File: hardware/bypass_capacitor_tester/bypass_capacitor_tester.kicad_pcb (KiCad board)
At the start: 2 copper layers, 40 x 34 mm, 13 parts, among them J1 Coax, J2 Coax, J3 Coax, J4 Conn_01x02, Q1 MMBT2369AL

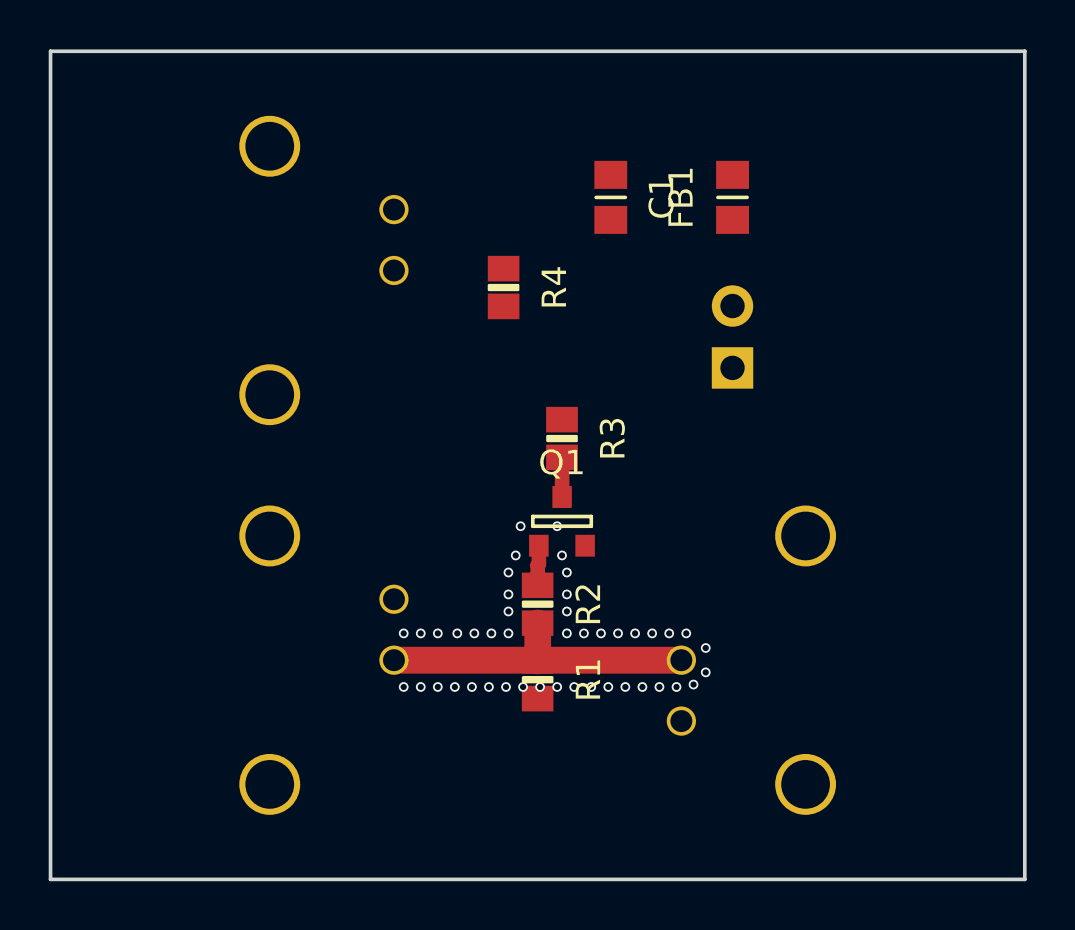
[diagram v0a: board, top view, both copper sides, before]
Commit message: changed coaxial connectors to SMA edge connectors
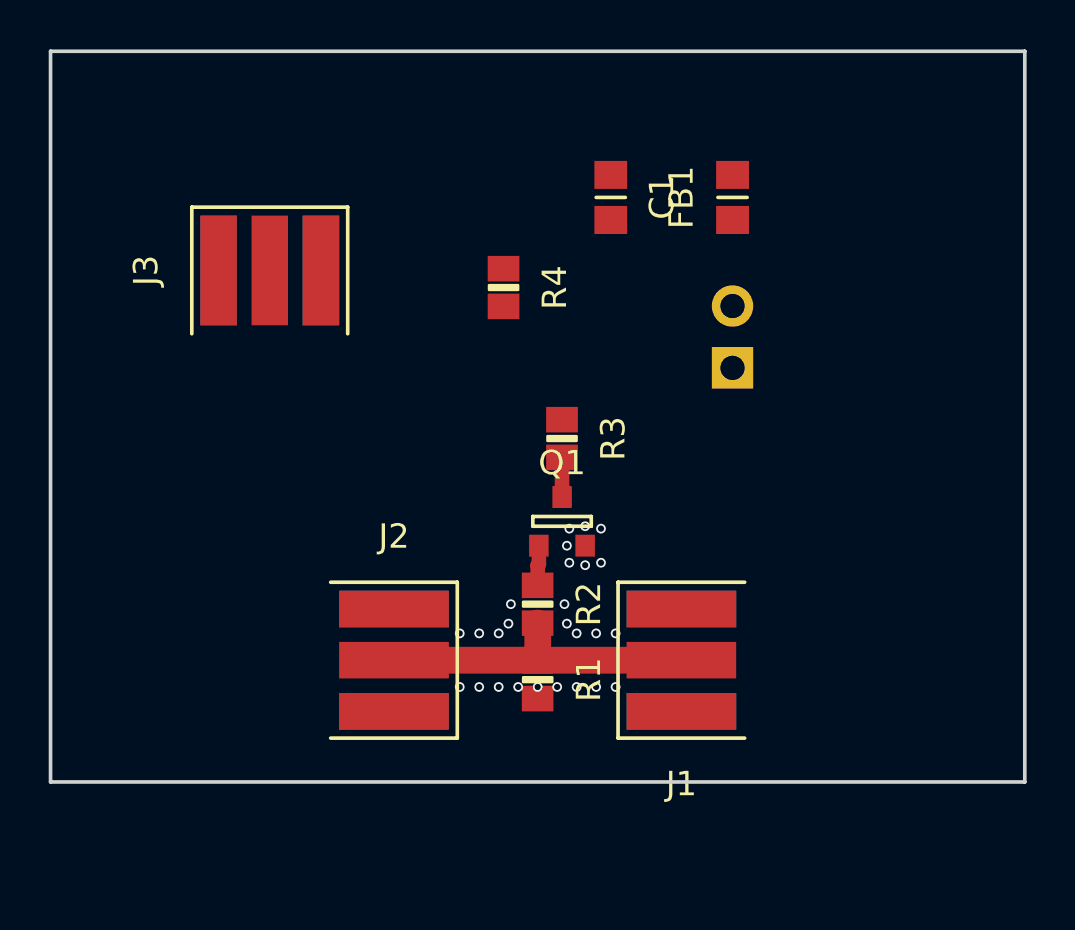
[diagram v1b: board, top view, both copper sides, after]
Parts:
- J1, J2, J3: footprint SquantorConnectors:Conn_BNC_RightAngle_TH -> SquantorConnectors:SMA_edge_6mm2; moved to F.Cu
- moved J1 5.10 mm to (192.9, 92.0), turned to 180 degrees
- moved J2 5.10 mm to (181.1, 92.0), turned to 0 degrees
- turned J3 to 90 degrees
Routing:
- net GND: vias 45 -> 26
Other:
- board size 40 x 34 mm -> 40 x 30 mm

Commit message: further placement
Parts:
- moved J3 7.95 mm to (181.1, 82.1), turned to 0 degrees
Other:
- board size 40 x 30 mm -> 28.5 x 30 mm
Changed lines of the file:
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@@
   (general
     (thickness 1.6)
-    (drawings 4)
+    (drawings 5)
     (tracks 33)
     (zones 0)
@@
   )
   (setup
-    (last_trace_width 0.6)
+    (last_trace_width 1.5)
     (user_trace_width 0.1524)
     (user_trace_width 0.2)
@@
   )
   (module SquantorConnectors:SMA_edge_6mm2 (layer F.Cu)
-    (at 176 76 90)
-    (fp_text reference J3 (at 0 -5.08 -90) (layer F.SilkS)
-      (effects (font (size 1 1) (thickness 0.15)))
-    )
-    (fp_text value Coax (at 0 4.445 -90) (layer F.Fab)
+    (at 181.1 82.1)
+    (fp_text reference J3 (at 0 -5.08 180) (layer F.SilkS)
+      (effects (font (size 1 1) (thickness 0.15)))
+    )
+    (fp_text value Coax (at 0 4.445 180) (layer F.Fab)
       (effects (font (size 1 1) (thickness 0.15)))
     )
@@
     (fp_line (start -2.6 -3.2) (end 2.6 -3.2) (layer F.SilkS) (width 0.15))
     (fp_line (start -2.6 -3.2) (end -2.6 3.2) (layer Dwgs.User) (width 0.1))
-    (pad 2 smd rect (at 0 2.1 90) (size 4.5 1.5) (layers B.Cu B.Paste B.Mask)
-      (net 2 GND))
-    (pad 2 smd rect (at 0 -2.1 90) (size 4.5 1.5) (layers B.Cu B.Paste B.Mask)
-      (net 2 GND))
-    (pad 2 smd rect (at 0 2.1 90) (size 4.5 1.5) (layers F.Cu F.Paste F.Mask)
-      (net 2 GND))
-    (pad 2 smd rect (at 0 -2.1 90) (size 4.5 1.5) (layers F.Cu F.Paste F.Mask)
-      (net 2 GND))
-    (pad 1 smd rect (at 0 0 90) (size 4.5 1.5) (layers F.Cu F.Paste F.Mask)
+    (pad 2 smd rect (at 0 2.1) (size 4.5 1.5) (layers B.Cu B.Paste B.Mask)
+      (net 2 GND))
+    (pad 2 smd rect (at 0 -2.1) (size 4.5 1.5) (layers B.Cu B.Paste B.Mask)
+      (net 2 GND))
+    (pad 2 smd rect (at 0 2.1) (size 4.5 1.5) (layers F.Cu F.Paste F.Mask)
+      (net 2 GND))
+    (pad 2 smd rect (at 0 -2.1) (size 4.5 1.5) (layers F.Cu F.Paste F.Mask)
+      (net 2 GND))
+    (pad 1 smd rect (at 0 0) (size 4.5 1.5) (layers F.Cu F.Paste F.Mask)
       (net 1 /B_WAVEFORM))
   )
@@
     )
   )
-  (gr_line (start 167 67) (end 167 97) (layer Edge.Cuts) (width 0.15))
-  (gr_line (start 207 67) (end 167 67) (layer Edge.Cuts) (width 0.15))
+  (gr_line (start 183.4 92) (end 190.7 92) (layer F.Mask) (width 1.3))
+  (gr_line (start 178.5 67) (end 178.5 97) (layer Edge.Cuts) (width 0.15))
+  (gr_line (start 207 67) (end 178.5 67) (layer Edge.Cuts) (width 0.15))
   (gr_line (start 207 97) (end 207 67) (layer Edge.Cuts) (width 0.15))
-  (gr_line (start 167 97) (end 207 97) (layer Edge.Cuts) (width 0.15))
+  (gr_line (start 178.5 97) (end 207 97) (layer Edge.Cuts) (width 0.15))
   (via (at 187 93.1) (size 0.4) (drill 0.254) (layers F.Cu B.Cu) (net 2))
   (via (at 183.8 93.1) (size 0.4) (drill 0.254) (layers F.Cu B.Cu) (net 2))
@@
     (polygon
       (pts
-        (xy 167 67) (xy 207 67) (xy 207 97) (xy 167 97)
+        (xy 178.5 67) (xy 207 67) (xy 207 97) (xy 178.5 97)
       )
     )
@@
     (polygon
       (pts
-        (xy 167 67) (xy 207 67) (xy 207 97) (xy 167 97)
+        (xy 178.5 67) (xy 207 67) (xy 207 97) (xy 178.5 97)
       )
     )

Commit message: further placement
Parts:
- J4: footprint Connector_PinHeader_2.54mm:PinHeader_1x02_P2.54mm_Horizontal -> Connector_PinHeader_2.54mm:PinHeader_1x03_P2.54mm_Horizontal
- moved N1 17.8 mm to (186.9, 91.7)
- moved N2 17.8 mm to (186.4, 95.7)
- moved FB1 10.8 mm to (187.1, 80.3), turned to 180 degrees
- moved R4 6.22 mm to (186.1, 82.9)
- moved J4 5.12 mm to (191.0, 83.2)
- moved C1 5.08 mm to (185.0, 73.9), turned to 90 degrees
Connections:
- J4 pad 2: VDD -> (no net)
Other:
- board size 28.5 x 30 mm -> 17 x 30 mm

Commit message: further placement
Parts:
- moved C1 12.2 mm to (193.1, 83.0), turned to 270 degrees
- moved J4 10.7 mm to (183.8, 75.3)
- moved FB1 0.92 mm to (187.7, 79.6), turned to 270 degrees
- moved Q1 0.30 mm to (187.7, 86.3)
- moved R3 0.30 mm to (187.7, 82.9)
- moved R4 0.30 mm to (185.8, 82.9)
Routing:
- net Net-(Q1-Pad1): track 1.65 -> 0.00 mm
- net Net-(Q1-Pad3): track 1.62 -> 0.00 mm
- net GND: vias 26 -> 19
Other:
- board size 17 x 30 mm -> 17 x 28.8 mm
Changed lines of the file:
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@@
     (thickness 1.6)
     (drawings 5)
-    (tracks 33)
+    (tracks 22)
     (zones 0)
     (modules 13)
@@
   )
   (module Connector_PinHeader_2.54mm:PinHeader_1x03_P2.54mm_Horizontal (layer B.Cu)
-    (at 191 83.2)
+    (at 183.8 75.3)
     (descr "Through hole angled pin header, 1x03, 2.54mm pitch, 6mm pin length, single row")
     (tags "Through hole angled pin header THT 1x03 2.54mm single row")
@@
   )
   (module SquantorRcl:R_0805+0603 (layer F.Cu)
-    (at 186.1 82.9 270)
+    (at 185.8 82.9 270)
     (descr "Resistor SMD 0805, reflow soldering, Vishay (see dcrcw.pdf)")
     (tags "resistor 0805")
@@
   )
   (module SquantorRcl:R_0805+0603 (layer F.Cu)
-    (at 188 82.9 270)
+    (at 187.7 82.9 270)
     (descr "Resistor SMD 0805, reflow soldering, Vishay (see dcrcw.pdf)")
     (tags "resistor 0805")
@@
   )
   (module SquantorIC:SOT23-3 (layer F.Cu)
-    (at 188 86.3)
+    (at 187.7 86.3)
     (fp_text reference Q1 (at 0 -2.4) (layer F.SilkS)
       (effects (font (size 1 1) (thickness 0.15)))
@@
   )
   (module SquantorRcl:C_0805+0603 (layer F.Cu)
-    (at 187.1 80.3 180)
+    (at 187.7 79.6 270)
     (descr "Capacitor SMD 0805 and 0603 pad sizes, reflow soldering, based on AVX dimensions")
     (tags "capacitor 0805 0603 mixed")
     (attr smd)
-    (fp_text reference FB1 (at 0 -2.1) (layer F.SilkS)
-      (effects (font (size 1 1) (thickness 0.15)))
-    )
-    (fp_text value Ferrite_Bead (at 0 2.1) (layer F.Fab)
+    (fp_text reference FB1 (at 0 -2.1 90) (layer F.SilkS)
+      (effects (font (size 1 1) (thickness 0.15)))
+    )
+    (fp_text value Ferrite_Bead (at 0 2.1 90) (layer F.Fab)
       (effects (font (size 1 1) (thickness 0.15)))
     )
@@
     (fp_line (start -1.75 -0.95) (end -1.75 0.95) (layer F.CrtYd) (width 0.05))
     (fp_line (start 1.75 -0.95) (end 1.75 0.95) (layer F.CrtYd) (width 0.05))
-    (pad 1 smd rect (at -0.925 0 180) (size 1.15 1.35) (layers F.Cu F.Paste F.Mask)
+    (pad 1 smd rect (at -0.925 0 270) (size 1.15 1.35) (layers F.Cu F.Paste F.Mask)
       (net 3 VDD))
-    (pad 2 smd rect (at 0.925 0 180) (size 1.15 1.35) (layers F.Cu F.Paste F.Mask)
+    (pad 2 smd rect (at 0.925 0 270) (size 1.15 1.35) (layers F.Cu F.Paste F.Mask)
       (net 1 /B_WAVEFORM))
     (model ${KISYS3DMOD}/Capacitor_SMD.3dshapes/C_0805_2012Metric.step
@@
   )
   (module SquantorRcl:C_0805+0603 (layer F.Cu)
-    (at 185 73.925 90)
+    (at 193.1 83 270)
     (descr "Capacitor SMD 0805 and 0603 pad sizes, reflow soldering, based on AVX dimensions")
     (tags "capacitor 0805 0603 mixed")
@@
     (fp_line (start -1.75 -0.95) (end -1.75 0.95) (layer F.CrtYd) (width 0.05))
     (fp_line (start 1.75 -0.95) (end 1.75 0.95) (layer F.CrtYd) (width 0.05))
-    (pad 1 smd rect (at -0.925 0 90) (size 1.15 1.35) (layers F.Cu F.Paste F.Mask)
+    (pad 1 smd rect (at -0.925 0 270) (size 1.15 1.35) (layers F.Cu F.Paste F.Mask)
       (net 1 /B_WAVEFORM))
-    (pad 2 smd rect (at 0.925 0 90) (size 1.15 1.35) (layers F.Cu F.Paste F.Mask)
+    (pad 2 smd rect (at 0.925 0 270) (size 1.15 1.35) (layers F.Cu F.Paste F.Mask)
       (net 2 GND))
     (model ${KISYS3DMOD}/Capacitor_SMD.3dshapes/C_0805_2012Metric.step
@@
   )
   (gr_line (start 183.4 92) (end 190.7 92) (layer F.Mask) (width 1.3))
-  (gr_line (start 178.5 67) (end 178.5 97) (layer Edge.Cuts) (width 0.15))
-  (gr_line (start 195.5 67) (end 178.5 67) (layer Edge.Cuts) (width 0.15))
-  (gr_line (start 195.5 97) (end 195.5 67) (layer Edge.Cuts) (width 0.15))
+  (gr_line (start 178.5 68.2) (end 178.5 97) (layer Edge.Cuts) (width 0.15))
+  (gr_line (start 195.5 68.2) (end 178.5 68.2) (layer Edge.Cuts) (width 0.15))
+  (gr_line (start 195.5 97) (end 195.5 68.2) (layer Edge.Cuts) (width 0.15))
   (gr_line (start 178.5 97) (end 195.5 97) (layer Edge.Cuts) (width 0.15))
   (via (at 187 93.1) (size 0.4) (drill 0.254) (layers F.Cu B.Cu) (net 2))
@@
   (via (at 189.4 90.9) (size 0.4) (drill 0.254) (layers F.Cu B.Cu) (net 2))
   (via (at 190.2 90.9) (size 0.4) (drill 0.254) (layers F.Cu B.Cu) (net 2))
-  (via (at 188.2 87.3) (size 0.4) (drill 0.254) (layers F.Cu B.Cu) (net 2))
-  (via (at 188.3 86.6) (size 0.4) (drill 0.254) (layers F.Cu B.Cu) (net 2))
-  (via (at 188.95 86.5) (size 0.4) (drill 0.254) (layers F.Cu B.Cu) (net 2))
-  (via (at 188.95 88.1) (size 0.4) (drill 0.254) (layers F.Cu B.Cu) (net 2))
-  (via (at 188.3 88) (size 0.4) (drill 0.254) (layers F.Cu B.Cu) (net 2))
-  (via (at 189.6 88) (size 0.4) (drill 0.254) (layers F.Cu B.Cu) (net 2))
-  (via (at 189.6 86.6) (size 0.4) (drill 0.254) (layers F.Cu B.Cu) (net 2))
   (segment (start 181.1 92) (end 192.9 92) (width 1.1) (layer F.Cu) (net 4))
   (segment (start 187 91.4) (end 187 92.025) (width 0.6) (layer F.Cu) (net 4))
   (segment (start 187 90.475) (end 187 91.4) (width 1.1) (layer F.Cu) (net 4))
-  (segment (start 188 85.3) (end 188 83.675) (width 0.6) (layer F.Cu) (net 5))
-  (segment (start 187.05 87.3) (end 187.05 88.05) (width 0.6) (layer F.Cu) (net 6))
-  (segment (start 187 88.1) (end 187 88.925) (width 0.6) (layer F.Cu) (net 6))
-  (segment (start 187.05 88.05) (end 187 88.1) (width 0.6) (layer F.Cu) (net 6))
   (zone (net 2) (net_name GND) (layer F.Cu) (hatch edge 0.508)
     (connect_pads yes (clearance 0.3))
@@
     (polygon
       (pts
-        (xy 178.5 67) (xy 195.5 67) (xy 195.5 97) (xy 178.5 97)
+        (xy 178.5 68.2) (xy 195.5 68.2) (xy 195.5 97) (xy 178.5 97)
       )
     )
@@
     (polygon
       (pts
-        (xy 178.5 67) (xy 195.5 67) (xy 195.5 97) (xy 178.5 97)
+        (xy 178.5 68.2) (xy 195.5 68.2) (xy 195.5 97) (xy 178.5 97)
       )
     )

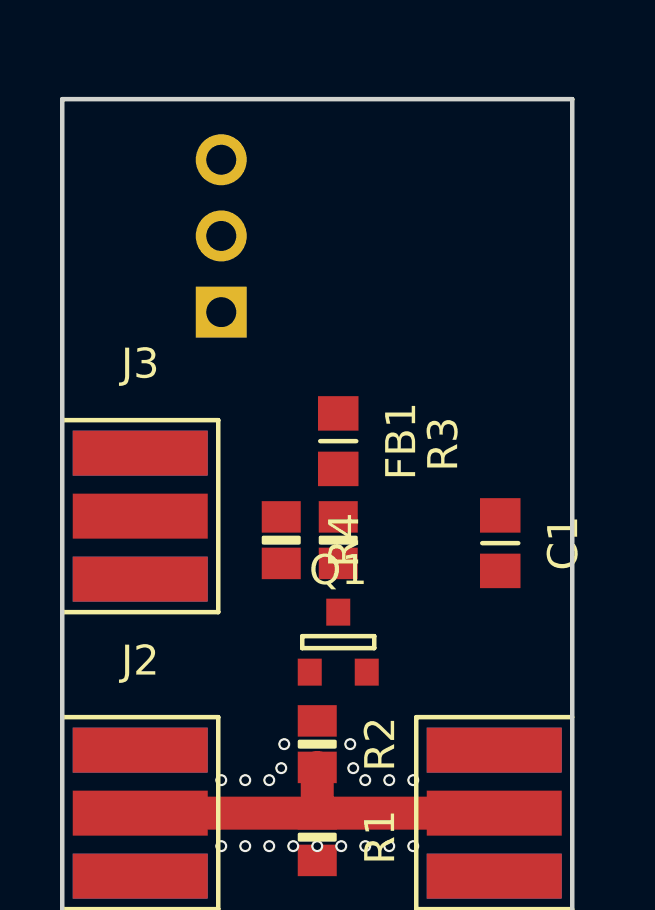
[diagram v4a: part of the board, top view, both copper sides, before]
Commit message: changed dut footprint, placement completed
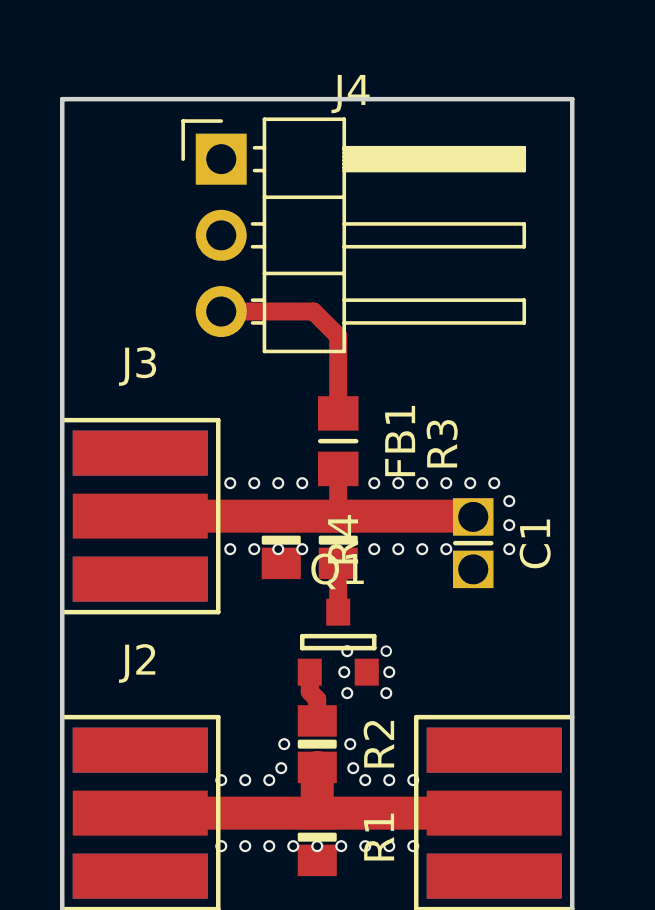
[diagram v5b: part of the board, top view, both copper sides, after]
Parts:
- C1: footprint SquantorRcl:C_0805+0603 -> SquantorRcl:C_TH+0805+0603+0402
- J4: moved to F.Cu
- moved N1 20.0 mm to (190.3, 72.0)
- moved N2 20.0 mm to (189.8, 76.0)
- moved J4 5.10 mm to (183.8, 70.2)
- moved C1 0.90 mm to (192.2, 83.0)
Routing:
- net /B_WAVEFORM: track 0.00 -> 12.7 mm
- net VDD: track 0.00 -> 6.81 mm
- net Net-(Q1-Pad1): track 0.00 -> 1.73 mm
- net Net-(Q1-Pad3): track 0.00 -> 1.62 mm
- net GND: vias 19 -> 46

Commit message: silk placement completed
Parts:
- J1: value Coax -> Pulse in
- J2: value Coax -> Pulse out
- J3: value Coax -> Output
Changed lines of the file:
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@@
     (tags "capacitor 0805 0603 0402 Through hole mixed")
     (attr smd)
-    (fp_text reference C1 (at 0 -2.1 90) (layer F.SilkS)
-      (effects (font (size 1 1) (thickness 0.15)))
-    )
-    (fp_text value DUT (at 0 2.1 90) (layer F.Fab)
+    (fp_text reference C1 (at -3.3 0 90) (layer F.SilkS)
+      (effects (font (size 1 1) (thickness 0.15)))
+    )
+    (fp_text value DUT (at 0 -2.3 90) (layer F.SilkS)
       (effects (font (size 1 1) (thickness 0.15)))
     )
@@
     (descr "Through hole angled pin header, 1x03, 2.54mm pitch, 6mm pin length, single row")
     (tags "Through hole angled pin header THT 1x03 2.54mm single row")
-    (fp_text reference J4 (at 4.385 -2.27) (layer F.SilkS)
+    (fp_text reference J4 (at -3 2.5) (layer F.SilkS)
       (effects (font (size 1 1) (thickness 0.15)))
     )
@@
   (module SquantorConnectors:SMA_edge_6mm2 (layer F.Cu)
     (at 181.1 82.1)
-    (fp_text reference J3 (at 0 -5.08 180) (layer F.SilkS)
-      (effects (font (size 1 1) (thickness 0.15)))
-    )
-    (fp_text value Coax (at 0 4.445 180) (layer F.Fab)
+    (fp_text reference J3 (at 0 -3.9 180) (layer F.SilkS)
+      (effects (font (size 1 1) (thickness 0.15)))
+    )
+    (fp_text value Output (at 0 4.2 180) (layer F.SilkS)
       (effects (font (size 1 1) (thickness 0.15)))
     )
@@
   (module SquantorConnectors:SMA_edge_6mm2 (layer F.Cu)
     (at 181.1 92)
-    (fp_text reference J2 (at 0 -5.08 180) (layer F.SilkS)
-      (effects (font (size 1 1) (thickness 0.15)))
-    )
-    (fp_text value Coax (at 0 4.445 180) (layer F.Fab)
+    (fp_text reference J2 (at 0 -3.9 180) (layer F.SilkS)
+      (effects (font (size 1 1) (thickness 0.15)))
+    )
+    (fp_text value "Pulse out" (at 1.1 4.2 180) (layer F.SilkS)
       (effects (font (size 1 1) (thickness 0.15)))
     )
@@
   (module SquantorConnectors:SMA_edge_6mm2 (layer F.Cu)
     (at 192.9 92 180)
-    (fp_text reference J1 (at 0 -5.08 180) (layer F.SilkS)
-      (effects (font (size 1 1) (thickness 0.15)))
-    )
-    (fp_text value Coax (at 0 4.445 180) (layer F.Fab)
+    (fp_text reference J1 (at 0 4.3 180) (layer F.SilkS)
+      (effects (font (size 1 1) (thickness 0.15)))
+    )
+    (fp_text value "Pulse in" (at 0.7 -4.1 180) (layer F.SilkS)
       (effects (font (size 1 1) (thickness 0.15)))
     )
@@
     (tags "resistor 0805")
     (attr smd)
-    (fp_text reference R4 (at 0 -2.1 90) (layer F.SilkS)
-      (effects (font (size 1 1) (thickness 0.15)))
-    )
-    (fp_text value 50 (at 0 2.1 90) (layer F.Fab)
+    (fp_text reference R4 (at 2.5 1.2 90) (layer F.SilkS)
+      (effects (font (size 1 1) (thickness 0.15)))
+    )
+    (fp_text value 50 (at -3 1.2 90) (layer F.SilkS)
       (effects (font (size 1 1) (thickness 0.15)))
     )
@@
     (tags "resistor 0805")
     (attr smd)
-    (fp_text reference R3 (at -3.2 -3.5 90) (layer F.SilkS)
-      (effects (font (size 1 1) (thickness 0.15)))
-    )
-    (fp_text value 100 (at 0 2.1 90) (layer F.Fab)
+    (fp_text reference R3 (at 1.4 -1.7 90) (layer F.SilkS)
+      (effects (font (size 1 1) (thickness 0.15)))
+    )
+    (fp_text value 100 (at -3.5 -1.7 90) (layer F.SilkS)
       (effects (font (size 1 1) (thickness 0.15)))
     )
@@
     (tags "resistor 0805")
     (attr smd)
-    (fp_text reference R2 (at 0 -2.1 90) (layer F.SilkS)
-      (effects (font (size 1 1) (thickness 0.15)))
-    )
-    (fp_text value 560 (at 0 2.1 90) (layer F.Fab)
+    (fp_text reference R2 (at 0 -2.2 90) (layer F.SilkS)
+      (effects (font (size 1 1) (thickness 0.15)))
+    )
+    (fp_text value 560 (at 0 2.1 90) (layer F.SilkS)
       (effects (font (size 1 1) (thickness 0.15)))
     )
@@
     (tags "resistor 0805")
     (attr smd)
-    (fp_text reference R1 (at 0 -2.1 90) (layer F.SilkS)
-      (effects (font (size 1 1) (thickness 0.15)))
-    )
-    (fp_text value 50 (at 0 2.1 90) (layer F.Fab)
+    (fp_text reference R1 (at 1.4 -2.2 90) (layer F.SilkS)
+      (effects (font (size 1 1) (thickness 0.15)))
+    )
+    (fp_text value 50 (at 1.5 2.1 90) (layer F.SilkS)
       (effects (font (size 1 1) (thickness 0.15)))
     )
@@
   (module SquantorIC:SOT23-3 (layer F.Cu)
     (at 187.7 86.3)
-    (fp_text reference Q1 (at 0 -2.4) (layer F.SilkS)
+    (fp_text reference Q1 (at 2.8 0) (layer F.SilkS)
       (effects (font (size 1 1) (thickness 0.15)))
     )
@@
     (tags "capacitor 0805 0603 mixed")
     (attr smd)
-    (fp_text reference FB1 (at 0 -2.1 90) (layer F.SilkS)
-      (effects (font (size 1 1) (thickness 0.15)))
-    )
-    (fp_text value Ferrite_Bead (at 0 2.1 90) (layer F.Fab)
-      (effects (font (size 1 1) (thickness 0.15)))
-    )
+    (fp_text reference FB1 (at -0.1 1.6 90) (layer F.SilkS)
+      (effects (font (size 1 1) (thickness 0.15)))
+    )
+    (fp_text value Ferrite_Bead (at -0.6 -4.1 90) (layer F.Fab) hide
+      (effects (font (size 1 1) (thickness 0.15)))
+    )

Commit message: updated versionnumber
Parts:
- N2: value 20191105 -> 20191112
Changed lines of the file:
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@@
       (effects (font (size 1 1) (thickness 0.15)) (justify mirror))
     )
-    (fp_text value 20191105 (at -0.4 0.1) (layer B.SilkS)
+    (fp_text value 20191112 (at -0.4 0.1) (layer B.SilkS)
       (effects (font (size 1 1) (thickness 0.15)) (justify mirror))
     )
